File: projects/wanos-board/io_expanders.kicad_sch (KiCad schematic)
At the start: 10 parts, among them U1 PCA9554PW, U2 PCA9554PW

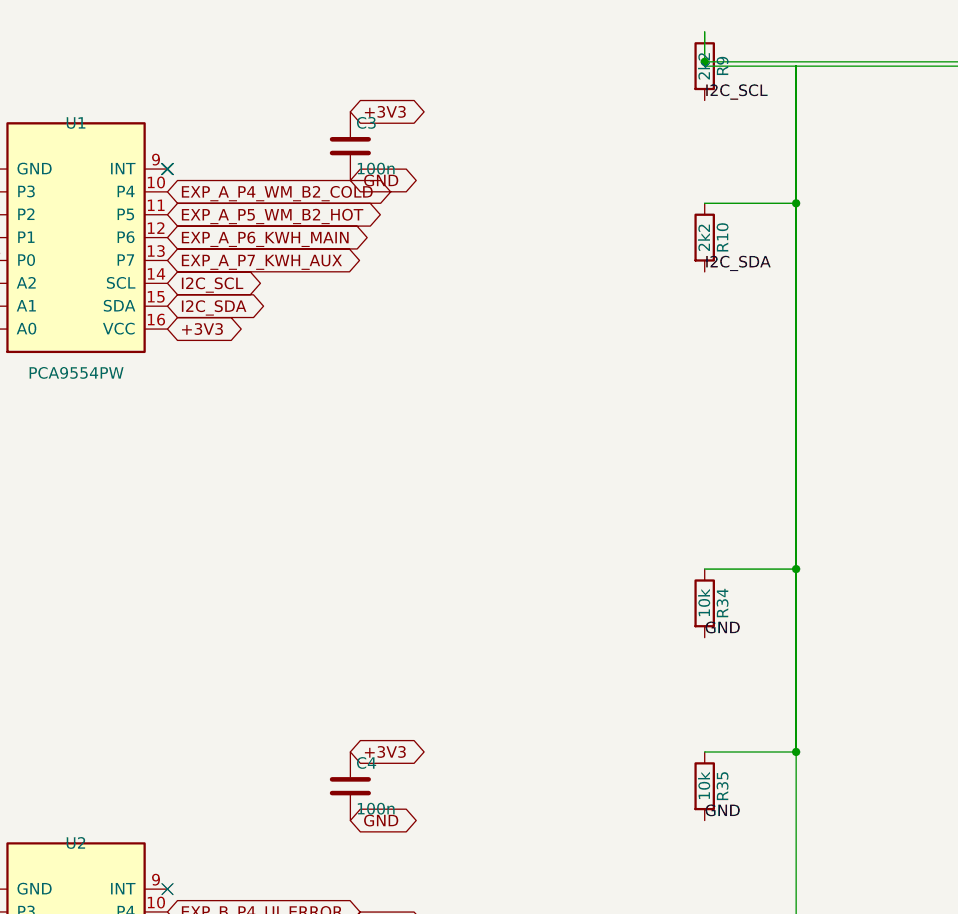
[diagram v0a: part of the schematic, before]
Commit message: pi_power & 12V_monitor schematics OK added datasheets doc update
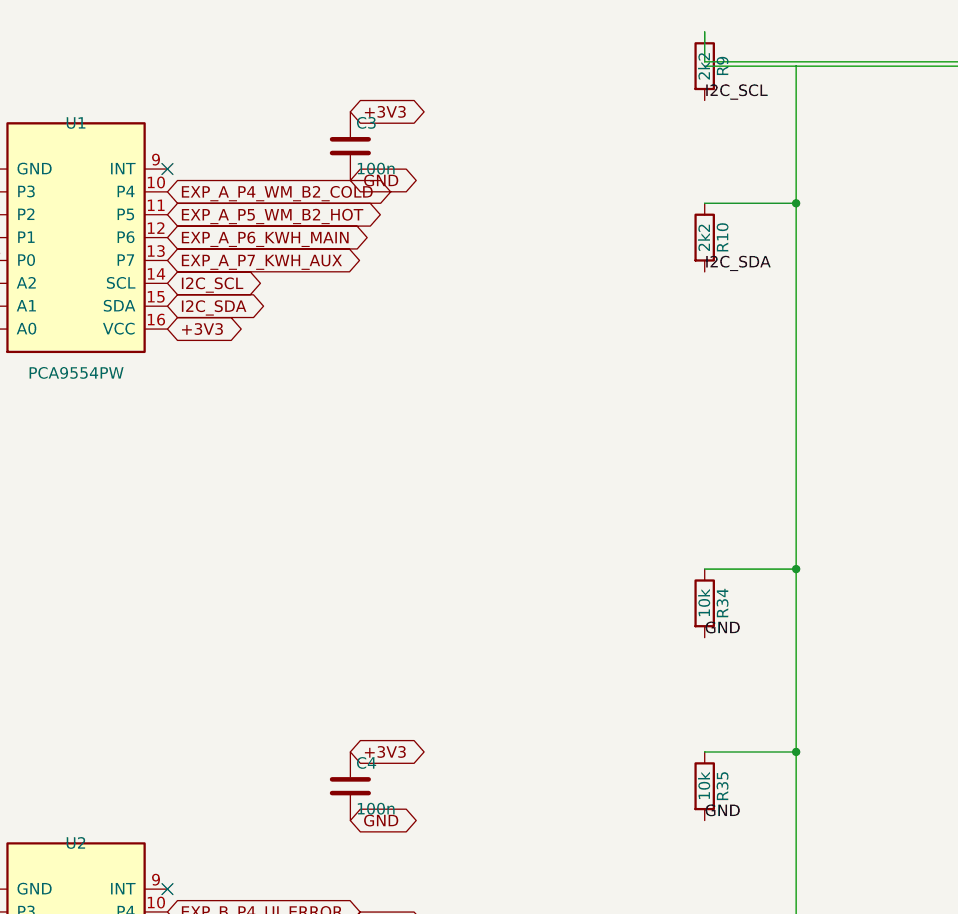
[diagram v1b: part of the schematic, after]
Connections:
- no-connect marks 8 -> 6

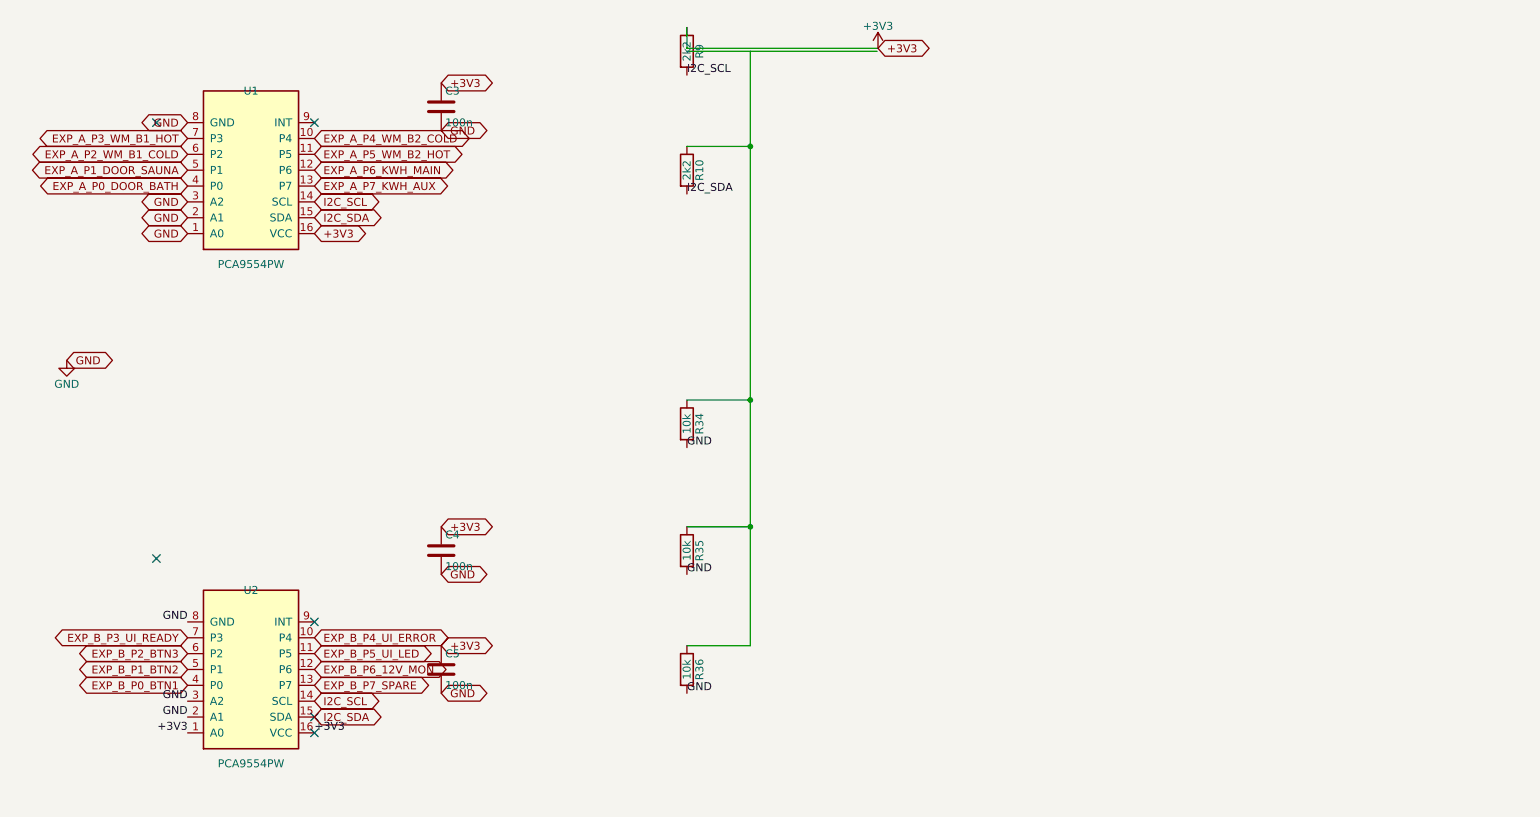
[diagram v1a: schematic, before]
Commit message: SSR, power, IO_expander schemas update
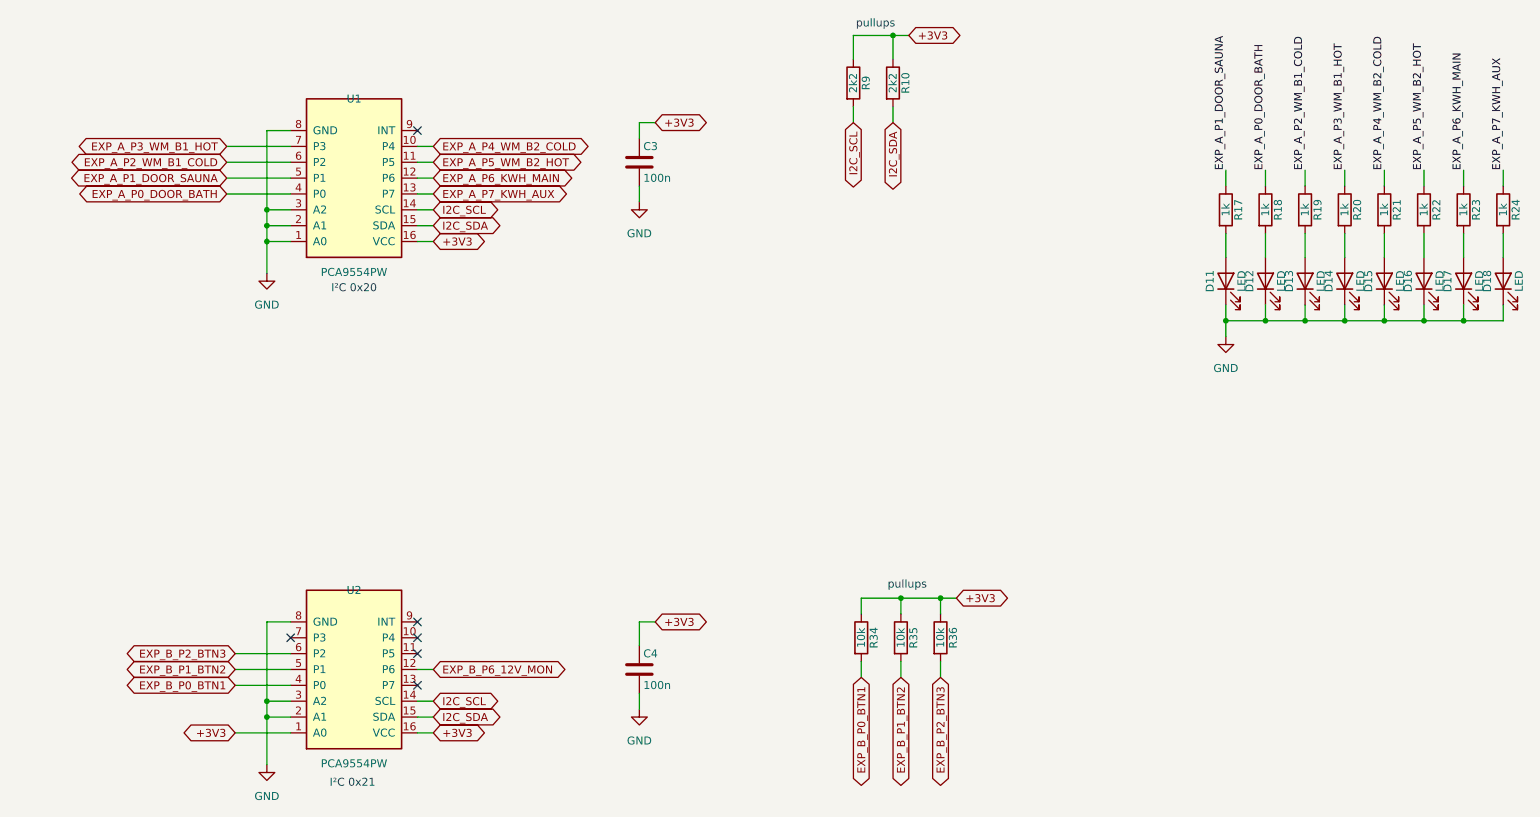
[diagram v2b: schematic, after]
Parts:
- removed C5: 100n, Capacitor_SMD:C_0805_2012Metric, symbol Device:C
- added D11, D12, D13, D14, D15, D16, D17, D18: LED, LED_SMD:LED_0805_2012Metric, symbol Device:LED
- added R17, R18, R19, R20, R21, R22, R23, R24: 1k, Resistor_SMD:R_0805_2012Metric, symbol Device:R
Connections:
- net +3V3: now also R10.1, R34.1, R35.1, R36.1
- net EXP_A_P0_DOOR_BATH: now also R18.1
- net EXP_A_P1_DOOR_SAUNA: now also R17.1
- net EXP_A_P2_WM_B1_COLD: now also R19.1
- net EXP_A_P3_WM_B1_HOT: now also R20.1
- net EXP_A_P4_WM_B2_COLD: now also R21.1
- net EXP_A_P5_WM_B2_HOT: now also R22.1
- net EXP_A_P6_KWH_MAIN: now also R23.1
- net EXP_A_P7_KWH_AUX: now also R24.1
- net EXP_B_P0_BTN1: now also R34.2
- net EXP_B_P1_BTN2: now also R35.2
- net EXP_B_P2_BTN3: now also R36.2
- net GND: now also D11.1 (K), D12.1 (K), D13.1 (K), D14.1 (K), D15.1 (K), D16.1 (K), D17.1 (K), D18.1 (K); no longer R34.2, R35.2, R36.2
- net EXP_B_P3_UI_READY: no longer names the net of U2.7 (P3)
- net EXP_B_P4_UI_ERROR: no longer names the net of U2.10 (P4)
- net EXP_B_P5_UI_LED: no longer names the net of U2.11 (P5)
- net EXP_B_P7_SPARE: no longer names the net of U2.13 (P7)
- new net: D14.2 (A), R20.2
- new net: D13.2 (A), R19.2
- new net: D17.2 (A), R23.2
- new net: D15.2 (A), R21.2
- new net: D18.2 (A), R24.2
- new net: D16.2 (A), R22.2
- new net: D12.2 (A), R18.2
- new net: D11.2 (A), R17.2
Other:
- note added: "I²C 0x20"
- note added: "I²C 0x21"
- note added: "pullups"
- moved on the sheet: C3, C4, R10, R9, U1, U2

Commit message: 1st draft: water meters schematic
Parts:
- removed D13, D14, D15, D16: LED, LED_SMD:LED_0805_2012Metric, symbol Device:LED
- removed R19, R20, R21, R22: 1k, Resistor_SMD:R_0805_2012Metric, symbol Device:R

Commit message: schema updates
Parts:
- added C18, C19, C20, C21: 100n, Capacitor_SMD:C_0805_2012Metric, symbol Device:C
- added D13, D14, D15, D16: LED, LED_SMD:LED_0805_2012Metric, symbol Device:LED
- added D25, D26, D27, D28: PESD5V0S1BA, Diode_SMD:D_SOD-323, symbol Device:D_TVS
- added D29: SMBJ5.0A, Diode_SMD:D_SMB, symbol Device:D_TVS
- added J2: DOOR_SAUNA, Connector_JST:JST_XH_B2B-XH-A_1x02_P2.50mm_Vertical, symbol Connector_Generic:Conn_01x02
- added J3: DOOR_BATH, Connector_JST:JST_XH_B2B-XH-A_1x02_P2.50mm_Vertical, symbol Connector_Generic:Conn_01x02
- added J4: 5556416-1, Connector_RJ:RJ45_Amphenol_54602-x08_Horizontal, symbol Connector_Generic:Conn_01x08
- added J6: KWH_MAIN, Connector_JST:JST_XH_B2B-XH-A_1x02_P2.50mm_Vertical, symbol Connector_Generic:Conn_01x02
- added J7: KWH_AUX, Connector_JST:JST_XH_B2B-XH-A_1x02_P2.50mm_Vertical, symbol Connector_Generic:Conn_01x02
- added J8: BTN_SAUNA, Connector_JST:JST_XH_B4B-XH-A_1x04_P2.50mm_Vertical, symbol Connector_Generic:Conn_01x04
- added R19, R20, R21, R22: 1k0, Resistor_SMD:R_0805_2012Metric, symbol Device:R
- added R37, R38, R39, R40: 10k, Resistor_SMD:R_0805_2012Metric, symbol Device:R
- added R41, R42, R43, R44: 330, Resistor_SMD:R_0805_2012Metric, symbol Device:R
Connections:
- net +3V3: now also R10.2, R34.2, R35.2, R36.2, R9.2, R19.1, R20.1, R21.1, R22.1, R37.1, R38.1, R39.1, R40.1; no longer R10.1, R34.1, R35.1, R36.1, R9.1
- net EXP_A_P0_DOOR_BATH: now also J3.2 (Pin_2)
- net EXP_A_P1_DOOR_SAUNA: now also J2.2 (Pin_2)
- net EXP_A_P2_WM_B1_COLD: now also D13.2 (A), R41.2
- net EXP_A_P3_WM_B1_HOT: now also D14.2 (A), R42.2
- net EXP_A_P4_WM_B2_COLD: now also D15.2 (A), R43.2
- net EXP_A_P5_WM_B2_HOT: now also D16.2 (A), R44.2
- net EXP_A_P6_KWH_MAIN: now also J6.2 (Pin_2)
- net EXP_A_P7_KWH_AUX: now also J7.2 (Pin_2)
- net EXP_B_P0_BTN1: now also R34.1, J8.2 (Pin_2); no longer R34.2
- net EXP_B_P1_BTN2: now also R35.1, J8.3 (Pin_3); no longer R35.2
- net EXP_B_P2_BTN3: now also R36.1, J8.4 (Pin_4); no longer R36.2
- net GND: now also C18.2, C19.2, C20.2, C21.2, D25.2 (A2), D26.2 (A2), D27.2 (A2), D28.2 (A2), D29.2 (A2), J2.1 (Pin_1), J3.1 (Pin_1), J4.2 (Pin_2), J4.5 (Pin_5), J4.6 (Pin_6), J6.1 (Pin_1), J7.1 (Pin_1), J8.1 (Pin_1)
- net I2C_SCL: now also R9.1; no longer R9.2
- net I2C_SDA: now also R10.1; no longer R10.2
- new net: D16.1 (K), R22.2
- new net: D14.1 (K), R20.2
- new net: D13.1 (K), R19.2
- new net: D15.1 (K), R21.2
- new net +5VA: D29.1 (A1), J4.4 (Pin_4)
- new net WM_B1_COLD: C18.1, D25.1 (A1), J4.1 (Pin_1), R37.2, R41.1
- new net WM_B1_HOT: C19.1, D26.1 (A1), J4.3 (Pin_3), R38.2, R42.1
- new net WM_B2_COLD: C20.1, D27.1 (A1), J4.7 (Pin_7), R39.2, R43.1
- new net WM_B2_HOT: C21.1, D28.1 (A1), J4.8 (Pin_8), R40.2, R44.1
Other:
- note added: "B1 COLD"
- note added: "B1 HOT"
- note added: "B2 COLD"
- note added: "B2 HOT"
- title: (none) -> wanos-pcb-v1 IO Expanders
